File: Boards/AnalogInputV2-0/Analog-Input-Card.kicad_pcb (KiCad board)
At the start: 2 copper layers, 80 x 72 mm, 21 parts, among them IC1 PIC16F1783, J1 5Vdc Jumper, P1 AquaPicBus, P2 Inputs, P3 ICSP, P4 Power, P5 EARTH GROUND, Q1 AO3407A, U1 ST485EC, X1 8MHz

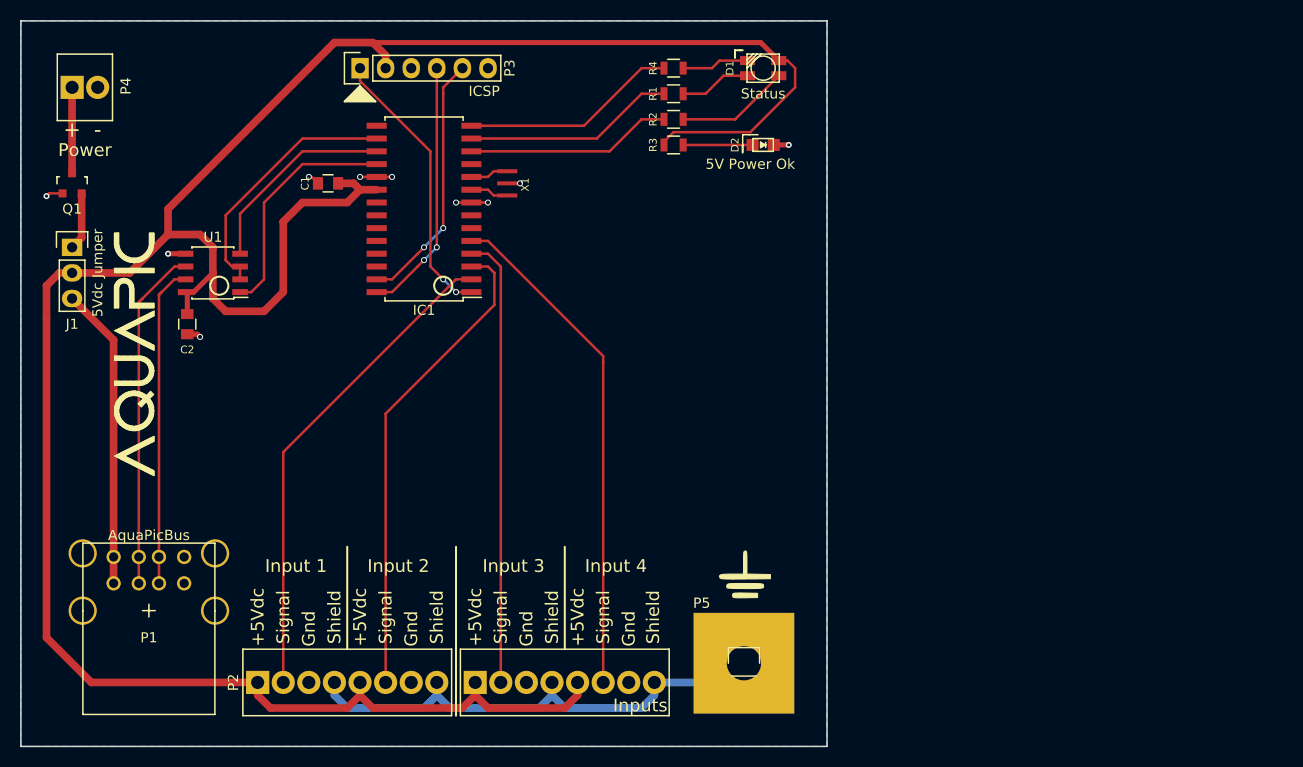
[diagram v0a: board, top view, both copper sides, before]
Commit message: worked on i2c driver and board design
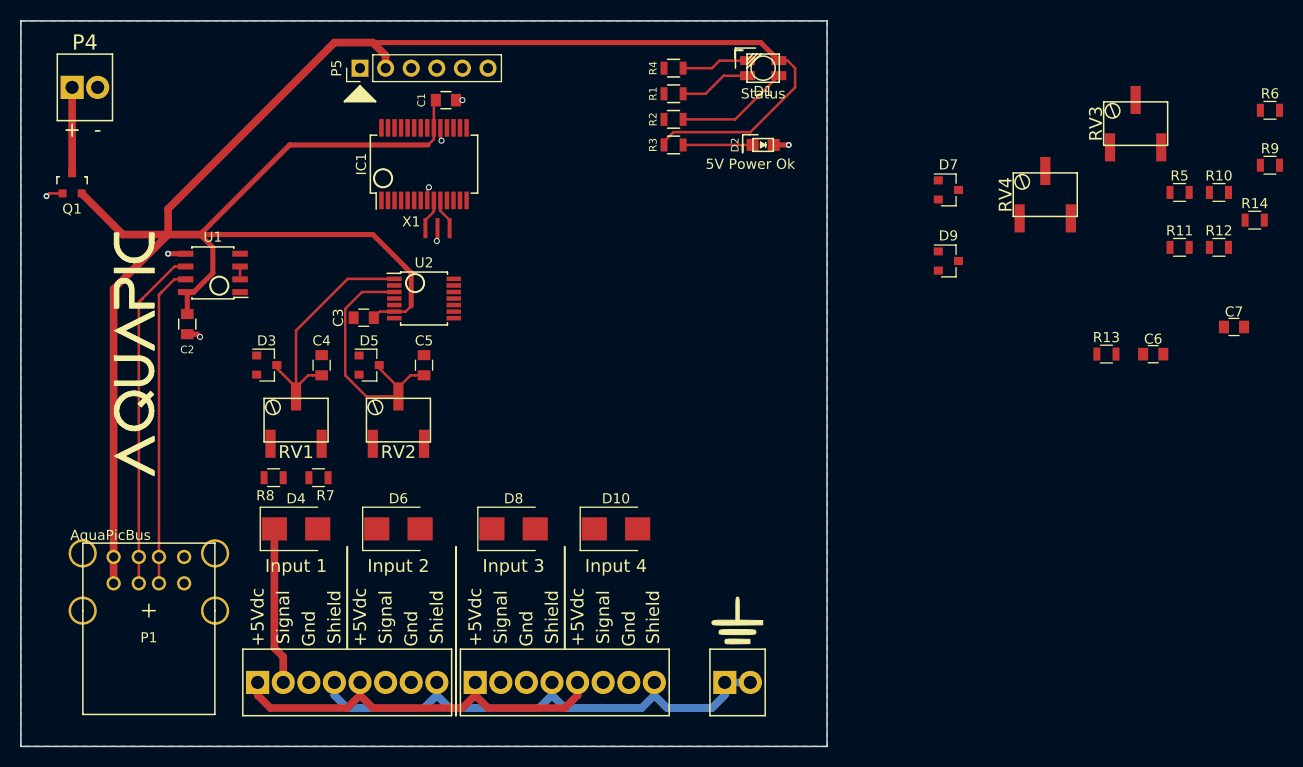
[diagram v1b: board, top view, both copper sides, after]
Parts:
- removed J1: 5Vdc Jumper, Pin_Headers:Pin_Header_Straight_1x03
- added C3: 100nF, Capacitors_SMD:C_0805, F.Cu at (34.0, -42.5)
- added C4: 100nF, Capacitors_SMD:C_0805, F.Cu at (29.8, -37.8)
- added C5: 100nF, Capacitors_SMD:C_0805, F.Cu at (40.0, -37.8)
- added C6: 100nF, Capacitors_SMD:C_0805, F.Cu at (112.4, -38.9)
- added C7: 100nF, Capacitors_SMD:C_0805, F.Cu at (120.4, -41.6)
- added D10: SMBJ30D, Diodes_SMD:D_SMB, F.Cu at (59.1, -21.6)
- added D3: BZX84C4V7, Diodes_SMD:D_SOT-23_ANK, F.Cu at (24.4, -37.8)
- added D4: SMBJ30D, Diodes_SMD:D_SMB, F.Cu at (27.3, -21.6)
- added D5: BZX84C4V7, Diodes_SMD:D_SOT-23_ANK, F.Cu at (34.6, -37.8)
- added D6: SMBJ30D, Diodes_SMD:D_SMB, F.Cu at (37.5, -21.6)
- added D7: BZX84C4V7, Diodes_SMD:D_SOT-23_ANK, F.Cu at (92.0, -55.2)
- added D8: SMBJ30D, Diodes_SMD:D_SMB, F.Cu at (48.9, -21.6)
- added D9: BZX84C4V7, Diodes_SMD:D_SOT-23_ANK, F.Cu at (92.0, -48.2)
- added R10: 10K, Resistors_SMD:R_0805, F.Cu at (118.9, -55.0)
- added R11: 4K32, Resistors_SMD:R_0805, F.Cu at (115.0, -49.5)
- added R12: 10K, Resistors_SMD:R_0805, F.Cu at (118.9, -49.5)
- added R13: 4K32, Resistors_SMD:R_0805, F.Cu at (107.7, -38.9)
- added R14: 10K, Resistors_SMD:R_0805, F.Cu at (122.4, -52.2)
- added R5: 4K32, Resistors_SMD:R_0805, F.Cu at (115.0, -55.0)
- added R6: 4K32, Resistors_SMD:R_0805, F.Cu at (124.0, -63.1)
- added R7: 4K32, Resistors_SMD:R_0805, F.Cu at (29.5, -26.7)
- added R8: 10K, Resistors_SMD:R_0805, F.Cu at (25.1, -26.7)
- added R9: 4K32, Resistors_SMD:R_0805, F.Cu at (124.0, -57.7)
- added RV1: 10K, MyFootPrints:POTENTIAMETER_SMD, F.Cu at (27.3, -32.4)
- added RV2: 10K, MyFootPrints:POTENTIAMETER_SMD, F.Cu at (37.5, -32.4)
- added RV3: 10K, MyFootPrints:POTENTIAMETER_SMD, F.Cu at (110.6, -61.8)
- added RV4: 10K, MyFootPrints:POTENTIAMETER_SMD, F.Cu at (101.7, -54.8)
- added U2: MCP3428, Housings_SSOP:TSSOP-14_4.4x5mm_Pitch0.65mm, F.Cu at (40.0, -44.5)
- D1: footprint A_MyFootPrints:PLCC-4 -> MyFootPrints:PLCC-4
- IC1: value PIC16F1783 -> PIC16F18855; footprint Housings_SOIC:SOIC-28_7.5x17.9mm_Pitch1.27mm -> Housings_SSOP:SSOP-28_5.3x10.2mm_Pitch0.65mm
- P1: footprint A_MyFootPrints:USB-1.1_Stacked -> MyFootPrints:USB-1.1_Stacked
- P2: footprint A_MyFootPrints:Screw_Header_1x16 -> MyFootPrints:Screw_Header_1x16
- P3: value ICSP -> Earth; footprint Pin_Headers:Pin_Header_Straight_1x06 -> MyFootPrints:Screw_Header_1x2
- P4: footprint A_MyFootPrints:Screw_Header_1x2 -> MyFootPrints:Screw_Header_1x2
- P5: value EARTH GROUND -> ICSP; footprint Pin_Headers:Pin_Header_Straight_1x01 -> Pin_Headers:Pin_Header_Straight_1x06_Pitch2.54mm
- X1: footprint A_MyFootPrints:Resonator_3.2x1.3 -> MyFootPrints:Resonator_3.2x1.3
- moved P3 71.6 mm to (71.1, -6.35), turned to 0 degrees
- moved P5 70.3 mm to (33.7, -67.3), turned to 90 degrees
- moved C1 14.3 mm to (42.2, -64.1), turned to 0 degrees
- moved X1 8.22 mm to (41.3, -51.4), turned to 180 degrees
- moved G*** 4.64 mm to (71.1, -11.4)
- moved IC1 4.44 mm to (40.0, -57.8), turned to 90 degrees
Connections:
- net /5Vdc renamed Net-(P4-Pad1)
- IC1 pad 12: /STAT_LED_Y -> Net-(IC1-Pad12)
- IC1 pad 13: /STAT_LED_G -> Net-(IC1-Pad13)
- IC1 pad 14: /STAT_LED_R -> /SCL
- IC1 pad 15: Net-(IC1-Pad15) -> /SDA
- IC1 pad 2: /Input1 -> /STAT_LED_R
- IC1 pad 3: /Input2 -> /STAT_LED_G
- IC1 pad 4: /Input3 -> /STAT_LED_Y
- IC1 pad 5: /Input4 -> Net-(IC1-Pad5)
- P1 pad 1: /5VdcB -> +5V
- P1 pad 5: /5VdcB -> +5V
- P2 pad 12: GNDPWR -> Net-(P2-Pad12)
- P2 pad 16: GNDPWR -> Net-(P2-Pad12)
- P2 pad 4: GNDPWR -> Net-(P2-Pad12)
- P2 pad 8: GNDPWR -> Net-(P2-Pad12)
- P3 pad 1: //MCLR -> Net-(P2-Pad12)
- P3 pad 2: +5V -> Net-(P2-Pad12)
- P5 pad 1: GNDPWR -> //MCLR
- Q1 pad 2: /5VdcA -> +5V
- X1 pad 1: Net-(IC1-Pad9) -> Net-(IC1-Pad10)
- X1 pad 3: Net-(IC1-Pad10) -> Net-(IC1-Pad9)
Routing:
- net Net-(P2-Pad12): track 0.00 -> 51.8 mm
- net /Input4: track 50.2 -> 0.00 mm
- net GNDPWR: track 49.7 -> 0.00 mm
- net /Input2: track 47.7 -> 0.00 mm
- net /Input3: track 44.7 -> 0.00 mm
- net /Input1: track 48.6 -> 15.6 mm
- net /5VdcB: track 30.0 -> 0.00 mm
- net //MCLR: track 27.7 -> 0.00 mm, vias 2 -> 0
- net /PGC: track 26.3 -> 0.00 mm, vias 2 -> 0
- net /PGD: track 25.6 -> 0.00 mm, vias 2 -> 0
- net /Ch1: track 0.00 -> 25.4 mm
- net /Ch2: track 0.00 -> 25.3 mm
- net /T_nR: track 25.5 -> 1.75 mm
- net /RX: track 23.3 -> 0.48 mm
- net /STAT_LED_R: track 21.5 -> 0.00 mm
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
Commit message: finished board layout for ai
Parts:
- added C10: 4u7, Capacitors_SMD:C_0805, F.Cu at (12.7, -67.3)
- added C8: 100nF, Capacitors_SMD:C_0805, F.Cu at (47.0, -55.9)
- added C9: 4u7, Capacitors_SMD:C_0805, F.Cu at (12.7, -62.9)
- added Q2: NX7002AK, TO_SOT_Packages_SMD:SOT-23, F.Cu at (23.5, -57.8)
- added Q3: NX7002AK, TO_SOT_Packages_SMD:SOT-23, F.Cu at (27.3, -46.4)
- added Q4: NX7002AK, TO_SOT_Packages_SMD:SOT-23, F.Cu at (27.3, -52.1)
- added R15: 4K99, Resistors_SMD:R_0805, F.Cu at (27.3, -57.8)
- added R16: 4K99, Resistors_SMD:R_0805, F.Cu at (19.7, -57.8)
- added R17: 4K99, Resistors_SMD:R_0805, F.Cu at (31.1, -46.4)
- added R18: 4K99, Resistors_SMD:R_0805, F.Cu at (23.5, -46.4)
- added R19: 1K, Resistors_SMD:R_0805, F.Cu at (31.8, -53.3)
- added R20: 10K, Resistors_SMD:R_0805, F.Cu at (31.8, -50.8)
- added R21: 10K, Resistors_SMD:R_0805, F.Cu at (23.5, -52.1)
- added U3: AP2114H, TO_SOT_Packages_SMD:SOT-223, F.Cu at (19.1, -65.4)
- D3, D5, D7, D9: value BZX84C4V7 -> BZX84C3V3
- IC1: value PIC16F18855 -> PIC32MM0064GPM028
- P2: value Inputs -> 2@ 8x1 2.54
- P3: value Earth -> 2x1 2.54
- P4: value Power -> 2x1 2.54
- Q1: footprint Housings_SOT-23_SOT-143_TSOT-6:SOT-23 -> TO_SOT_Packages_SMD:SOT-23
- R11, R13, R5, R6, R7, R9: value 4K32 -> 4K99
- moved R6 87.8 mm to (37.1, -50.2)
- moved R9 87.6 mm to (39.4, -34.9), turned to 180 degrees
- moved R10 85.7 mm to (35.6, -34.9)
- moved R12 73.4 mm to (47.0, -34.9)
- moved RV3 69.8 mm to (48.9, -29.2)
- moved R14 67.5 mm to (57.1, -34.9)
- moved R5 67.5 mm to (47.6, -50.2), turned to 180 degrees
- moved R11 65.8 mm to (50.8, -34.9), turned to 180 degrees
- moved C6 60.9 mm to (51.4, -38.7), turned to 90 degrees
- moved C7 58.9 mm to (61.6, -38.7), turned to 90 degrees
- moved RV4 49.7 mm to (59.1, -29.2)
- moved D7 48.9 mm to (46.0, -38.7)
- moved R13 46.9 mm to (61.0, -34.9), turned to 180 degrees
- moved D9 36.9 mm to (56.4, -38.6)
- moved C1 11.9 mm to (33.0, -56.5), turned to 180 degrees
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- renumbered P5 to P1, R4 to R3, R3 to R4
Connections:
- net /D+ renamed /A
- net /D- renamed /B
- C1 pad 1: +5V -> +3V3
- C3 pad 1: +5V -> +3V3
- D1 pad 4: +5V -> +3V3
- IC1 pad 1: //MCLR -> /LED_R
- IC1 pad 10: Net-(IC1-Pad10) -> +3V3
- IC1 pad 11: Net-(IC1-Pad11) -> /SDA
- IC1 pad 14: /SCL -> //RTS
- IC1 pad 15: /SDA -> //RTS
- IC1 pad 16: /T_nR -> /SCL
- IC1 pad 17: /TX -> Net-(C8-Pad1)
- IC1 pad 18: /RX -> Net-(IC1-Pad18)
- IC1 pad 19: GND -> Net-(IC1-Pad19)
- IC1 pad 2: /STAT_LED_R -> /LED_G
- IC1 pad 20: +5V -> Net-(IC1-Pad20)
- IC1 pad 22: Net-(IC1-Pad22) -> /TX_LV
- IC1 pad 23: Net-(IC1-Pad23) -> /RX_LV
- IC1 pad 24: Net-(IC1-Pad24) -> GND
- IC1 pad 25: Net-(IC1-Pad25) -> +3V3
- IC1 pad 26: Net-(IC1-Pad26) -> //MCLR
- IC1 pad 3: /STAT_LED_G -> /LED_Y
- IC1 pad 4: /STAT_LED_Y -> Net-(IC1-Pad4)
- IC1 pad 5: Net-(IC1-Pad5) -> GND
- IC1 pad 8: GND -> Net-(IC1-Pad8)
- P1 pad 2: +5V -> +3V3
- R1 pad 2: /STAT_LED_G -> /LED_G
- R10 pad 1: /Input2 -> GND
- R10 pad 2: Net-(R10-Pad2) -> /Ch2
- R11 pad 2: Net-(R11-Pad2) -> /Ch3
- R12 pad 1: /Input3 -> GND
- R12 pad 2: Net-(R11-Pad1) -> /Ch3
- R13 pad 2: Net-(R13-Pad2) -> /Ch4
- R14 pad 1: /Input4 -> GND
- R14 pad 2: Net-(R13-Pad1) -> /Ch4
- R2 pad 2: /STAT_LED_Y -> /LED_Y
- R3 pad 2: /STAT_LED_R -> /LED_R
- R5 pad 1: +5V -> +3V3
- R6 pad 1: +5V -> +3V3
- R7 pad 2: Net-(R7-Pad2) -> /Ch1
- R8 pad 1: /Input1 -> GND
- R8 pad 2: Net-(R7-Pad1) -> /Ch1
- R9 pad 1: Net-(R10-Pad2) -> Net-(R9-Pad1)
- R9 pad 2: Net-(R9-Pad2) -> /Ch2
- RV1 pad 1: GND -> /Input1
- RV1 pad 2: /Ch1 -> Net-(R7-Pad1)
- RV1 pad 3: Net-(R7-Pad2) -> Net-(R7-Pad1)
- RV2 pad 1: GND -> /Input2
- RV2 pad 2: /Ch2 -> Net-(R9-Pad1)
- RV2 pad 3: Net-(R9-Pad2) -> Net-(R9-Pad1)
- RV3 pad 1: GND -> /Input3
- RV3 pad 2: /Ch3 -> Net-(R11-Pad1)
- RV3 pad 3: Net-(R11-Pad2) -> Net-(R11-Pad1)
- RV4 pad 1: GND -> /Input4
- RV4 pad 2: /Ch4 -> Net-(R13-Pad1)
- RV4 pad 3: Net-(R13-Pad2) -> Net-(R13-Pad1)
- U1 pad 2: /T_nR -> /RTS
- U1 pad 3: /T_nR -> /RTS
- U2 pad 6: +5V -> +3V3
- X1 pad 1: Net-(IC1-Pad10) -> Net-(IC1-Pad7)
- X1 pad 3: Net-(IC1-Pad9) -> Net-(IC1-Pad6)
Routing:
- net +3V3: track 0.00 -> 171.9 mm
- net GND: track 10.9 -> 53.6 mm, vias 8 -> 42
- net /LED_R: track 0.00 -> 29.9 mm, vias 0 -> 4
- net /LED_G: track 0.00 -> 29.1 mm, vias 0 -> 4
- net /LED_Y: track 0.00 -> 28.8 mm, vias 0 -> 4
- net /TX_LV: track 0.00 -> 27.7 mm, vias 0 -> 2
- net /Ch4: track 0.00 -> 25.2 mm
- net /RX_LV: track 0.00 -> 23.0 mm, vias 0 -> 2
- net /Input3: track 0.00 -> 21.0 mm
- net /Input2: track 0.00 -> 21.0 mm
- net /Input4: track 0.00 -> 21.0 mm
- net /Ch3: track 0.00 -> 18.9 mm
- net /SDA: track 0.00 -> 15.8 mm, vias 0 -> 2
- net /SCL: track 0.00 -> 14.7 mm, vias 0 -> 2
- net //MCLR: track 0.00 -> 14.4 mm, vias 0 -> 2
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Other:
- net class Default: clearance 0.2032 -> 0.1524
- rule trace_clearance: 0.2032 -> 0.1524
- board text added: "AquaPic Analog Input Rev 2.0 Goodtime Development"
- board text added: "ISCP"
- board text removed: "AquaPic Analog Input Rev 0.1 Skyler"

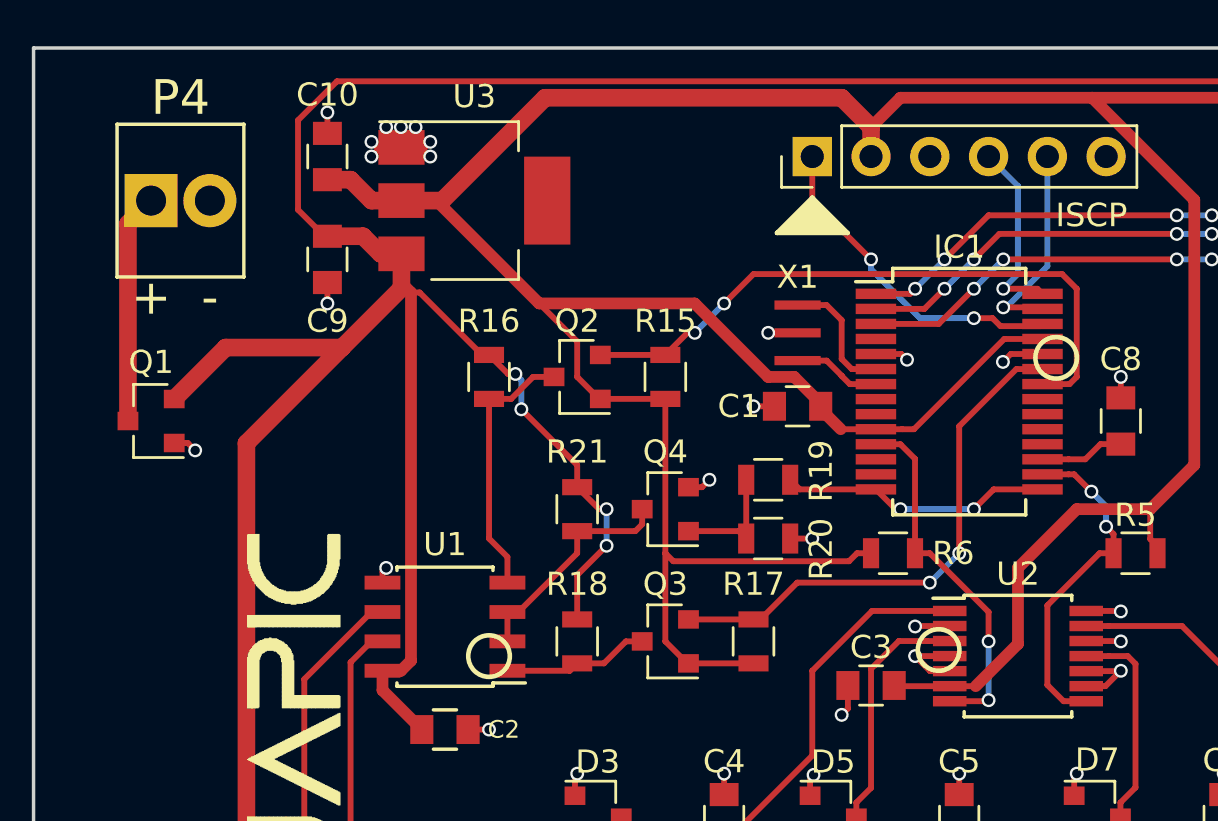
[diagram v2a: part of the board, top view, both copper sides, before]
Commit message: fixed silkscreen on analog input
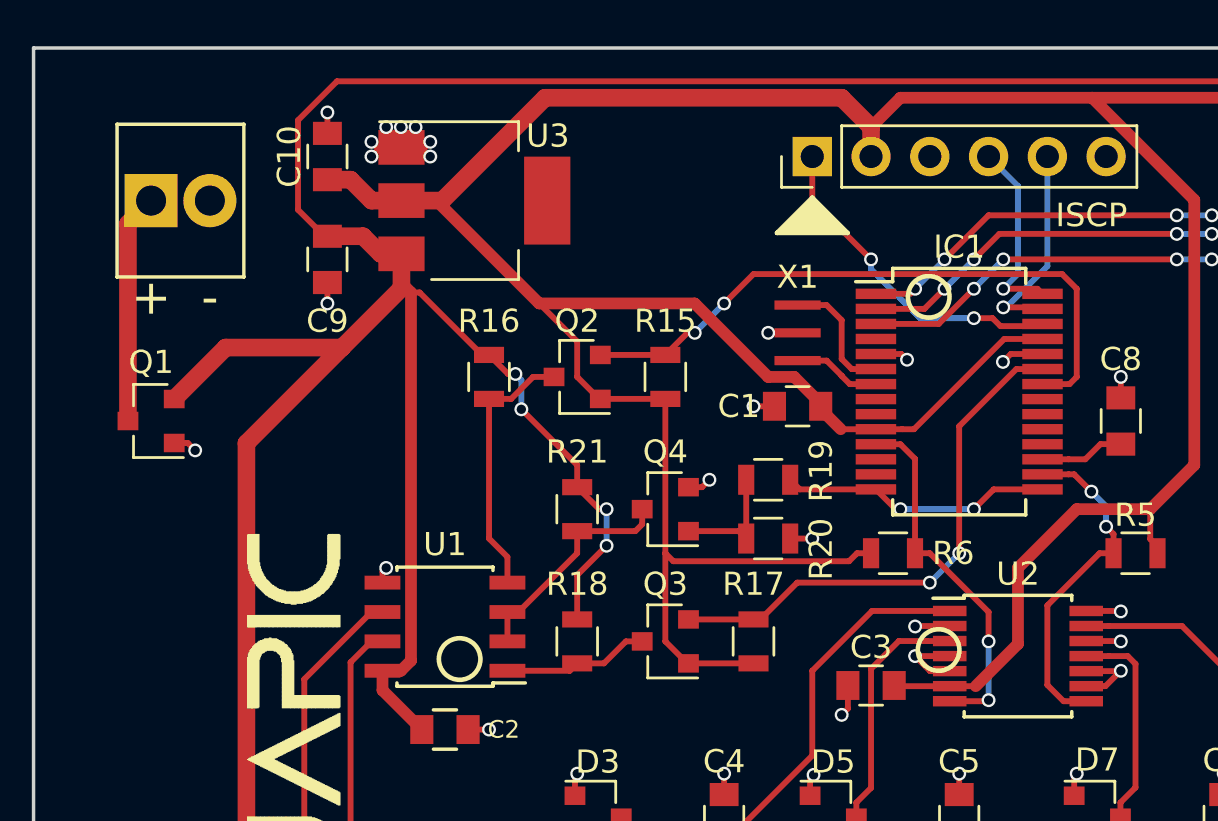
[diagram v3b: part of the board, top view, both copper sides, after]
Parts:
- P1: value ICSP -> 6x1 2.54
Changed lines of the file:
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@@
   )
   (setup
-    (last_trace_width 0.762)
+    (last_trace_width 0.254)
     (user_trace_width 0.508)
     (user_trace_width 0.762)
@@
       (usegerberextensions true)
       (excludeedgelayer true)
-      (linewidth 0.127000)
+      (linewidth 0.152400)
       (plotframeref false)
       (viasonmask false)
@@
   (module MyFootPrints:Screw_Header_1x2 (layer F.Cu)
     (at 6.35 -65.405)
-    (fp_text reference P4 (at 0 -4.445) (layer F.SilkS)
+    (fp_text reference P4 (at -1.27 -2.159) (layer F.SilkS) hide
       (effects (font (size 1.5 1.5) (thickness 0.15)))
     )
@@
       (effects (font (size 1 1) (thickness 0.15)))
     )
-    (fp_text value ICSP (at 0 6.35 180) (layer F.Fab)
+    (fp_text value "6x1 2.54" (at 0 6.35 180) (layer F.Fab)
       (effects (font (size 1 1) (thickness 0.15)))
     )
@@
     (tags "capacitor 0805")
     (attr smd)
-    (fp_text reference C10 (at 2.667 0 180) (layer F.SilkS)
+    (fp_text reference C10 (at 0 -1.651 270) (layer F.SilkS)
       (effects (font (size 1 1) (thickness 0.15)))
     )
@@
     (tags "CMS SOT")
     (attr smd)
-    (fp_text reference U3 (at 0 -4.5) (layer F.SilkS)
+    (fp_text reference U3 (at 3.175 -2.794) (layer F.SilkS)
       (effects (font (size 1 1) (thickness 0.15)))
     )
@@
     (effects (font (size 1.016 1.016) (thickness 0.2032)))
   )
-  (gr_circle (center 44.196 -58.6105) (end 44.831 -57.9755) (layer F.SilkS) (width 0.2))
+  (gr_circle (center 38.688 -61.2455) (end 39.323 -60.6105) (layer F.SilkS) (width 0.2))
   (gr_line (start 71.628 -58.928) (end 71.628 -59.69) (angle 90) (layer F.SilkS) (width 0.2))
-  (gr_circle (center 19.685 -45.72) (end 20.32 -45.085) (layer F.SilkS) (width 0.2))
+  (gr_circle (center 18.415 -45.593) (end 19.05 -44.958) (layer F.SilkS) (width 0.2))
   (gr_circle (center 39.116 -45.983025) (end 39.751 -45.348025) (layer F.SilkS) (width 0.2))
   (gr_text "AquaPic\nAnalog Input\nRev 2.0\nGoodtime Development" (at 64.77 -24.765) (layer B.SilkS)
